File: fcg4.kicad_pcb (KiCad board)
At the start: 4 copper layers, 34 x 33.5 mm, 98 parts, among them IC1 MP9943AGQ-Z, IC2 MP9943AGQ-Z, J1 USB4105-GF-A-120, J2 SM08B-SRSS-TB, U1 STM32G473CEUx, U10 MAX40200ANS_T, U11 MAX40200ANS_T, U2 ICM-42688-P, U4 AP2112K-3.3TRG1, U5 AP2112K-1.8TRG1, Y1 ECS-240-6-37B-7KM-TR

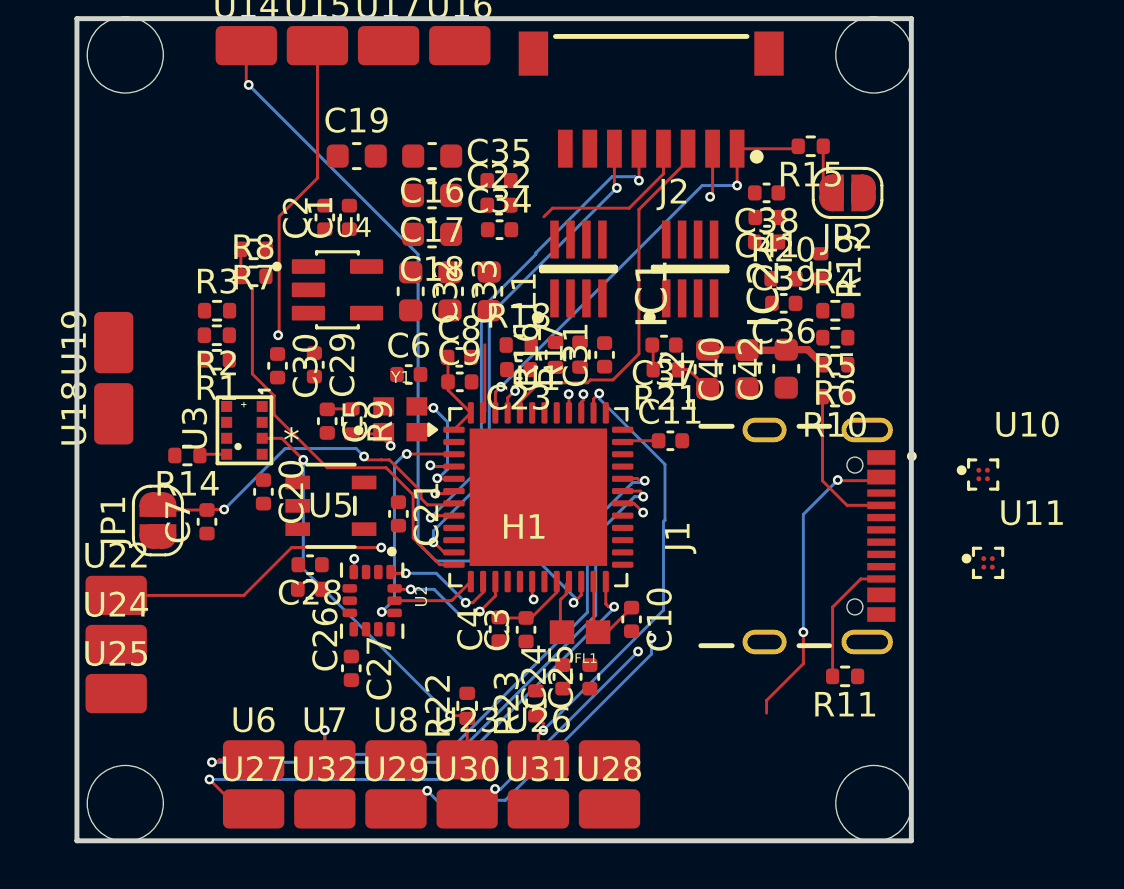
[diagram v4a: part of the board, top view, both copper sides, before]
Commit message: add 100ohm for pwm and some routing
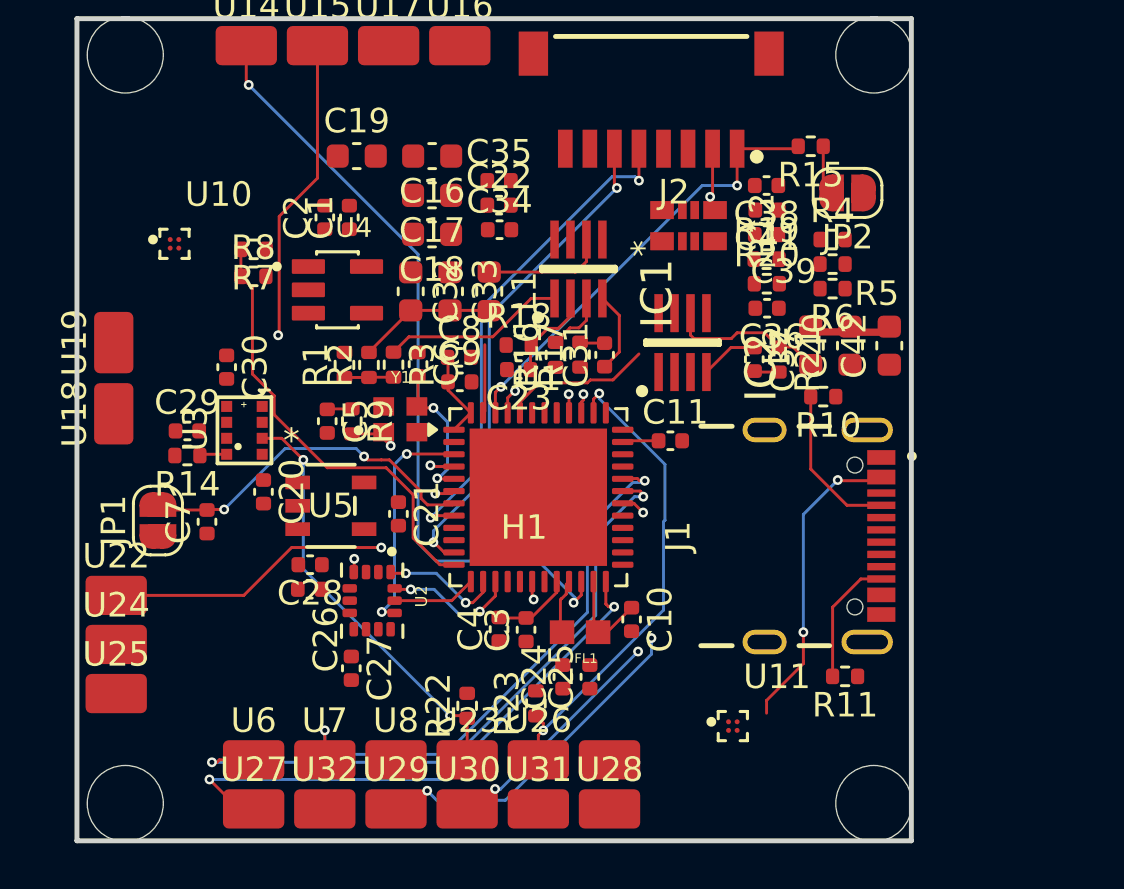
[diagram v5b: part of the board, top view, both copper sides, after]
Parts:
- added R12: EXB-28V101JX, fcg4_fp:EXB28V_PAN, F.Cu at (24.9, 8.94)
- R1: value 6.98k -> 7.68k
- moved U10 34.3 mm to (3.98, 9.68)
- moved U11 12.3 mm to (26.7, 29.3)
- moved R3 7.52 mm to (12.9, 14.6), turned to -90 degrees
- moved R2 6.32 mm to (11.9, 14.6), turned to 90 degrees
- moved C29 5.83 mm to (4.50, 17.3), turned to 0 degrees
- moved R1 5.20 mm to (10.9, 14.6), turned to 90 degrees
- moved R21 4.63 mm to (28.6, 14.4), turned to -90 degrees
- moved L2 4.31 mm to (29.9, 13.8)
- moved C40 4.31 mm to (31.5, 13.8)
- moved C42 4.30 mm to (33.1, 13.8)
- moved C37 3.73 mm to (27.6, 14.4), turned to -90 degrees
- moved R6 3.10 mm to (30.8, 11.5)
- moved IC2 3.02 mm to (24.7, 13.7)
- moved R5 3.00 mm to (30.8, 10.5)
- moved R4 2.90 mm to (30.8, 9.50)
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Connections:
- J2 pad 1: MOTOR1 -> /Connectors/MOTOR_1
- J2 pad 2: MOTOR2 -> /Connectors/MOTOR_2
- J2 pad 3: MOTOR3 -> /Connectors/MOTOR_3
- J2 pad 4: MOTOR4 -> /Connectors/MOTOR_4
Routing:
- net MOTOR3: track 15.3 -> 6.10 mm
- net /Power/FB_5V5: track 0.00 -> 7.47 mm
- net MOTOR4: track 9.43 -> 2.81 mm
- net 5V5_BEC: track 0.00 -> 5.62 mm
- net /Power/LC_5V5: track 0.00 -> 5.03 mm
- net /Power/LC_9V: track 1.52 -> 6.51 mm
- net /Power/BIAS_SUPPLY_5V5: track 0.00 -> 3.83 mm
- net /Power/BST_5V5: track 0.00 -> 3.31 mm
- net /Power/EN/SYNC_5V5: track 0.00 -> 2.53 mm
- net /Power/BST_9V: track 0.00 -> 2.36 mm
- net Net-(R1-Pad1): track 0.00 -> 2.00 mm
- net 9V_BEC: track 4.96 -> 3.22 mm
- net /MCU/OSC_IN: track 4.70 -> 5.96 mm
- net /Power/RC_BST_5V5: track 0.00 -> 1.02 mm

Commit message: routing...
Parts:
- moved U14 8.70 mm to (15.6, 1.60)
- moved U16 8.70 mm to (6.90, 1.60)
- moved U10 6.26 mm to (10.0, 11.3)
- moved R8 5.19 mm to (12.3, 11.9), turned to -90 degrees
- moved R7 5.10 mm to (12.3, 9.90), turned to -90 degrees
- moved C42 5.07 mm to (30.6, 9.40), turned to 0 degrees
- moved R4 5.05 mm to (29.6, 14.4), turned to 90 degrees
- moved U4 4.61 mm to (6.01, 11.8)
- moved R5 3.91 mm to (30.6, 14.4), turned to -90 degrees
- moved C19 3.49 mm to (14.5, 4.50), turned to 180 degrees
- moved R6 3.02 mm to (31.6, 14.4), turned to -90 degrees
- moved C40 2.96 mm to (30.6, 11.0), turned to 0 degrees
- moved U15 2.90 mm to (12.7, 1.60)
- moved U17 2.90 mm to (9.80, 1.60)
- moved C34 2.10 mm to (17.3, 7.00), turned to 180 degrees
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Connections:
- R12 pad 1: MOTOR1 -> /Connectors/MOTOR_1
- R12 pad 2: MOTOR2 -> /Connectors/MOTOR_2
- R12 pad 3: MOTOR3 -> /Connectors/MOTOR_3
- R12 pad 4: MOTOR4 -> /Connectors/MOTOR_4
- R12 pad 5: /Connectors/MOTOR_4 -> MOTOR4
- R12 pad 6: /Connectors/MOTOR_3 -> MOTOR3
- R12 pad 7: /Connectors/MOTOR_2 -> MOTOR2
- R12 pad 8: /Connectors/MOTOR_1 -> MOTOR1
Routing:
- net 9V_BEC: track 3.22 -> 29.7 mm, vias 0 -> 2
- net GND: track 0.00 -> 19.6 mm, vias 0 -> 8
- net MOTOR4: track 2.81 -> 12.0 mm
- net /Power/FB_9V: track 0.00 -> 7.27 mm
- net /Power/PG_5V5: track 0.00 -> 6.00 mm, vias 0 -> 2
- net MOTOR3: track 6.10 -> 11.4 mm
- net /Power/PG_9V: track 0.00 -> 4.92 mm
- net VDD_MCU: track 9.03 -> 13.1 mm
- net /Connectors/MOTOR_1: track 0.00 -> 2.87 mm
- net MOTOR2: track 27.5 -> 24.7 mm
- net /Connectors/MOTOR_2: track 0.00 -> 2.80 mm
- net /Connectors/MOTOR_3: track 0.48 -> 3.07 mm
- net /Connectors/MOTOR_4: track 0.00 -> 2.52 mm
- net TX3: track 31.7 -> 29.5 mm
- net /Power/LC_5V5: track 5.03 -> 7.23 mm, vias 0 -> 2
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- added copper zone on F.Cu, net +5V
- added copper zone on In1.Cu, net GND
- added copper zone on F.Cu, net VBAT
- added copper zone on F.Cu, net VCC_ICM

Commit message: routing...
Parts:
- moved R10 11.6 mm to (28.0, 27.2), turned to 0 degrees
- moved R11 11.5 mm to (30.1, 15.9)
- moved J1 3.08 mm to (31.1, 21.6), turned to 90 degrees
- moved U11 2.24 mm to (24.8, 28.2)
- moved R22 1.93 mm to (14.0, 28.9), turned to 180 degrees
- moved R23 1.28 mm to (17.7, 29.2), turned to 180 degrees
- moved R17 1.00 mm to (21.5, 14.2), turned to -90 degrees
- moved C31 1.00 mm to (20.5, 14.2), turned to -90 degrees
- moved U10 0.90 mm to (10.3, 12.1), turned to 180 degrees
- moved R9 0.77 mm to (10.6, 17.4), turned to 0 degrees
- moved C27 0.72 mm to (11.7, 26.5), turned to 0 degrees
- moved R12 0.70 mm to (24.9, 8.23)
- moved C5 0.65 mm to (10.6, 16.4), turned to 0 degrees
- moved U4 0.37 mm to (6.05, 11.5), turned to 90 degrees
- moved C11 0.34 mm to (23.9, 17.9)
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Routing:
- net GND: track 19.6 -> 75.9 mm, vias 8 -> 29
- net I2C1_SCL: track 19.8 -> 42.1 mm, vias 2 -> 4
- net /Power/BIAS_SUPPLY_9V: track 0.00 -> 8.40 mm, vias 0 -> 2
- net /MCU/USB_DIFF+: track 0.00 -> 7.92 mm
- net /MCU/USB_DIFF-: track 0.00 -> 7.91 mm
- net /Power/EN/SYNC_9V: track 0.00 -> 7.76 mm, vias 0 -> 2
- net 5V_USB: track 12.5 -> 5.08 mm, vias 2 -> 0
- net VDD_MCU: track 13.1 -> 18.4 mm, vias 0 -> 8
- net /Power/LC_5V5: track 7.23 -> 12.6 mm
- net 9V_BEC: track 29.7 -> 33.8 mm
- net MOTOR3: track 11.4 -> 14.5 mm, vias 0 -> 2
- net RX3: track 59.7 -> 56.7 mm, vias 3 -> 4
- net 5V5_BEC: track 5.62 -> 8.00 mm
- net /MCU/VDDA: track 2.24 -> 4.49 mm
- net /Power/LC_9V: track 4.91 -> 6.69 mm
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- added copper zone on In2.Cu, net VDD_MCU

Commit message: routing...
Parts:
- moved R22 2.14 mm to (16.0, 28.1), turned to 0 degrees
- moved U9 1.30 mm to (21.2, 29.5)
- moved U26 1.26 mm to (18.4, 29.5)
- moved U23 1.24 mm to (15.6, 29.5)
- moved U8 1.22 mm to (12.8, 29.5)
- moved U7 1.20 mm to (10.0, 29.5)
- moved U6 1.20 mm to (7.20, 29.5)
- moved R23 1.14 mm to (18.0, 28.1)
- moved U28 0.94 mm to (21.2, 31.9)
- moved U31 0.89 mm to (18.4, 31.9)
- moved U30 0.85 mm to (15.6, 31.9)
- moved U29 0.82 mm to (12.8, 31.9)
- moved U32 0.81 mm to (10.0, 31.9)
- moved U27 0.80 mm to (7.20, 31.9)
- turned R15 to 0 degrees
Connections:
- JP2 pad 1: GND -> VDD_MCU
- JP2 pad 2: /MCU/BOOT0 -> MOTOR1
- R15 pad 1: /MCU/BOOT0 -> GND
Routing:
- net GND: track 75.9 -> 70.3 mm, vias 29 -> 28
- net RX3: track 56.7 -> 52.9 mm
- net TX1: track 26.6 -> 23.7 mm
- net I2C1_SDA: track 28.8 -> 26.0 mm
- net MOTOR1: track 20.1 -> 22.2 mm
- net /MCU/BOOT0: track 1.90 -> 0.00 mm
- net VDD_MCU: track 18.4 -> 20.1 mm
- net RX1: track 22.6 -> 21.2 mm
- net I2C1_SCL: track 42.1 -> 43.5 mm
- net 9V_BEC: track 33.8 -> 34.9 mm
